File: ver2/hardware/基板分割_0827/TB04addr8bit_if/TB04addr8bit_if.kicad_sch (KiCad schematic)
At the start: 12 parts, among them J101 USB_C_Receptacle_PowerOnly_6P, SW101 SW_SPDT, U101 74LS157, U102 74HC138

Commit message: ver2: 3分割で丸ごと不要なシートを削除(ctrl 3・alu 8・if 9シート)
階層ピン0のシートのみ削除。RS00/RS01は22ピンあるためGUI待ち。
差分は追加0行の純削除。

Co-Authored-By: Claude Opus 5 <noreply@anthropic.com>
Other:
- removed sheet Decoder
- removed sheet InterFace
- removed sheet PC_aluMux (4 ページ)
- removed sheet ROM_ALU
- removed sheet addrDecord
- removed sheet addrMUX
- removed sheet gates
- removed sheet ram
- removed sheet sp

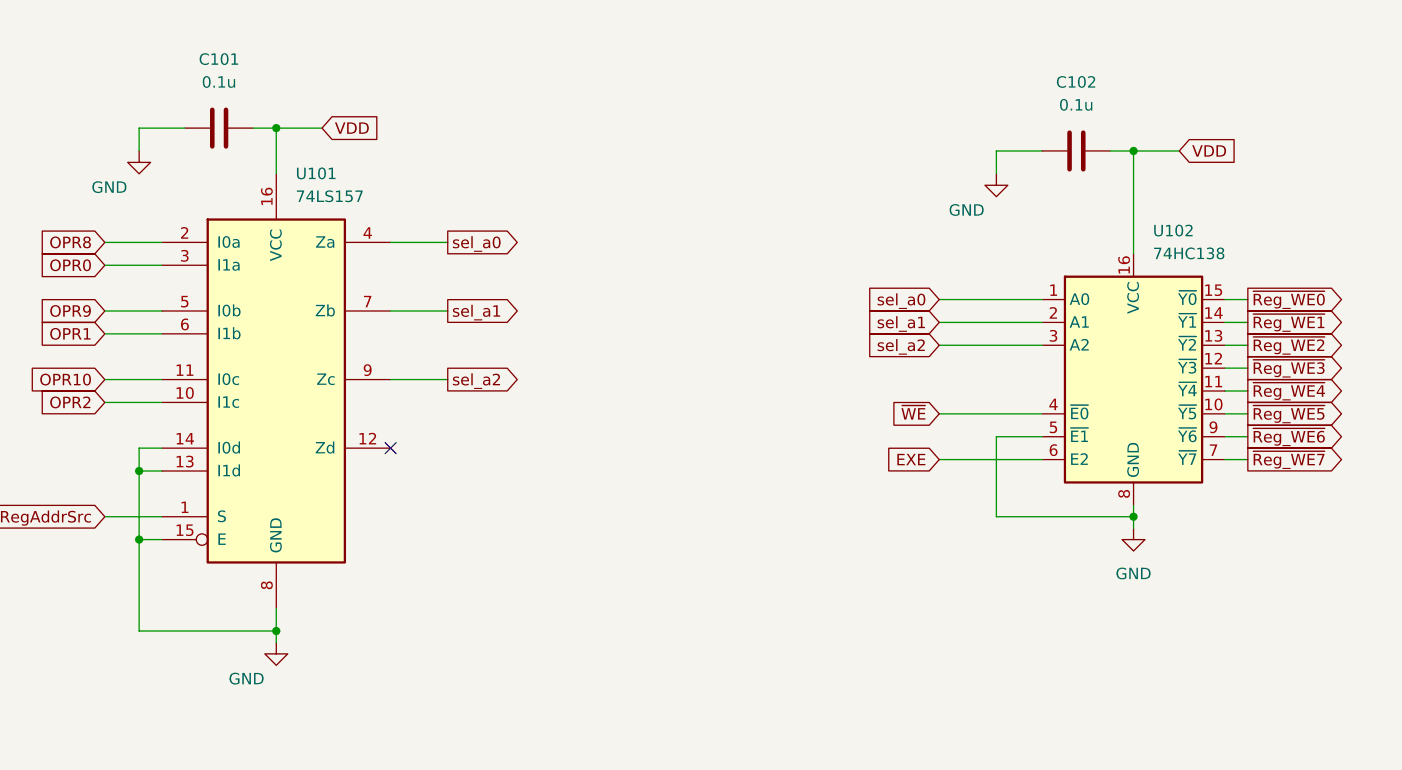
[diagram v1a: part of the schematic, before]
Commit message: ver2: 3分割で他基板側のICを削除(ctrl 9・alu 15・if 2個)
削除前にまたぎ本数(37/20)で割り当てを検算。kicad-cliのパース通過を確認。

Co-Authored-By: Claude Opus 5 <noreply@anthropic.com>
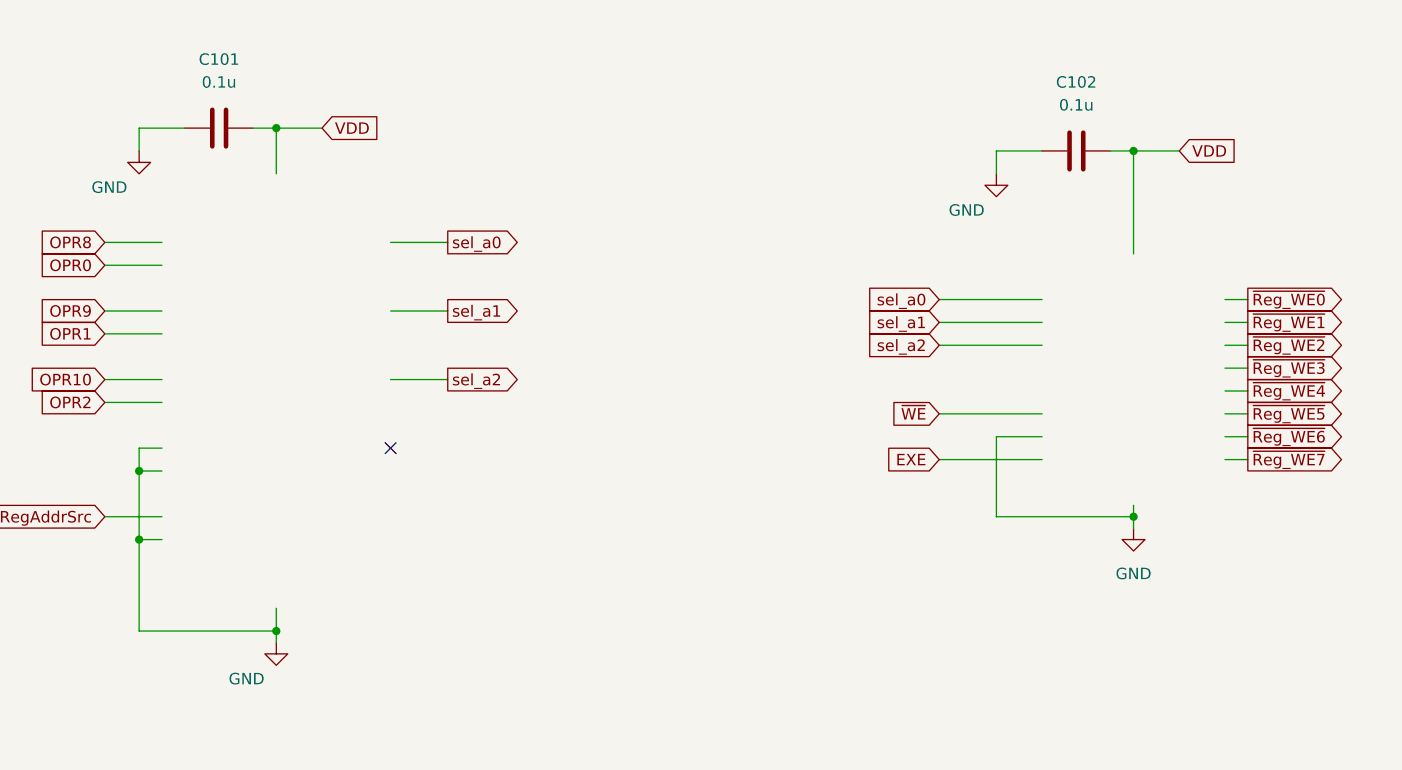
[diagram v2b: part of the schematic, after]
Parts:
- removed U101: 74LS157, Package_DIP:DIP-16_W7.62mm_Socket, symbol 74xx:74LS157
- removed U102: 74HC138, Package_DIP:DIP-16_W7.62mm_Socket, symbol 74xx:74HC138
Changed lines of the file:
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@@
-	)
-	(symbol
-		(lib_id "74xx:74LS157")
-		(at 171.45 146.05 0)
-		(unit 1)
-		(body_style 1)
-		(exclude_from_sim no)
-		(in_bom yes)
-		(on_board yes)
-		(in_pos_files yes)
-		(dnp no)
-		(fields_autoplaced yes)
-		(property "Reference" "U101"
-			(at 173.5933 123.19 0)
-			(show_name no)
-			(do_not_autoplace no)
-			(effects
-				(font
-					(size 1.27 1.27)
-				)
-				(justify left)
-			)
-		)
-		(property "Value" "74LS157"
-			(at 173.5933 125.73 0)
-			(show_name no)
-			(do_not_autoplace no)
-			(effects
-				(font
-					(size 1.27 1.27)
-				)
-				(justify left)
-			)
-		)
-		(property "Footprint" "Package_DIP:DIP-16_W7.62mm_Socket"
-			(at 171.45 146.05 0)
-			(hide yes)
-			(show_name no)
-			(do_not_autoplace no)
-			(effects
-				(font
-					(size 1.27 1.27)
-				)
-			)
-		)
-		(property "Datasheet" "http://www.ti.com/lit/gpn/sn74LS157"
-			(at 171.45 146.05 0)
-			(hide yes)
-			(show_name no)
-			(do_not_autoplace no)
-			(effects
-				(font
-					(size 1.27 1.27)
-				)
-			)
-		)
-		(property "Description" "Quad 2 to 1 line Multiplexer"
-			(at 171.45 146.05 0)
-			(hide yes)
-			(show_name no)
-			(do_not_autoplace no)
-			(effects
-				(font
-					(size 1.27 1.27)
-				)
-			)
-		)
-		(pin "4"
-		)
-		(pin "12"
-		)
-		(pin "6"
-		)
-		(pin "9"
-		)
-		(pin "3"
-		)
-		(pin "16"
-		)
-		(pin "8"
-		)
-		(pin "10"
-		)
-		(pin "11"
-		)
-		(pin "5"
-		)
-		(pin "13"
-		)
-		(pin "1"
-		)
-		(pin "2"
-		)
-		(pin "7"
-		)
-		(pin "14"
-		)
-		(pin "15"
-		)
-		(instances
-			(project "TB04addr8bit_if"
-				(path "/d176c79b-dced-4d01-bcec-7dfd676fcfc2"
-					(reference "U101")
-					(unit 1)
-				)
-			)
-		)
 	)
 	(symbol
@@
 					(unit 1)
 				)
-			)
-		)
-	)
-	(symbol
-		(lib_id "74xx:74HC138")
-		(at 266.7 147.32 0)
-		(unit 1)
-		(body_style 1)
-		(exclude_from_sim no)
-		(in_bom yes)
-		(on_board yes)
-		(in_pos_files yes)
-		(dnp no)
-		(fields_autoplaced yes)
-		(property "Reference" "U102"
-			(at 268.8433 129.54 0)
-			(show_name no)
-			(do_not_autoplace no)
-			(effects
-				(font
-					(size 1.27 1.27)
-				)
-				(justify left)
-			)
-		)
-		(property "Value" "74HC138"
-			(at 268.8433 132.08 0)
-			(show_name no)
-			(do_not_autoplace no)
-			(effects
-				(font
-					(size 1.27 1.27)
-				)
-				(justify left)
-			)
-		)
-		(property "Footprint" "Package_DIP:DIP-16_W7.62mm_Socket"
-			(at 266.7 147.32 0)
-			(hide yes)
-			(show_name no)
-			(do_not_autoplace no)
-			(effects
-				(font
-					(size 1.27 1.27)
-				)
-			)
-		)
-		(property "Datasheet" "http://www.ti.com/lit/ds/symlink/cd74hc238.pdf"
-			(at 266.7 147.32 0)
-			(hide yes)
-			(show_name no)
-			(do_not_autoplace no)
-			(effects
-				(font
-					(size 1.27 1.27)
-				)
-			)
-		)
-		(property "Description" "3-to-8 line decoder/multiplexer inverting, DIP-16/SOIC-16/SSOP-16"
-			(at 266.7 147.32 0)
-			(hide yes)
-			(show_name no)
-			(do_not_autoplace no)
-			(effects
-				(font
-					(size 1.27 1.27)
-				)
-			)
-		)
-		(pin "11"
-		)
-		(pin "1"
-		)
-		(pin "8"
-		)
-		(pin "5"
-		)
-		(pin "14"
-		)
-		(pin "10"
-		)
-		(pin "2"
-		)
-		(pin "4"
-		)
-		(pin "13"
-		)
-		(pin "3"
-		)
-		(pin "7"
-		)
-		(pin "6"
-		)
-		(pin "16"
-		)
-		(pin "12"
-		)
-		(pin "9"
-		)
-		(pin "15"
-		)
-		(instances
-			(project "TB04addr4bit"
-				(path "/4ea1f5c4-c9b0-4258-a3d4-23d6760fc0c5"
-					(reference "U15")
-					(unit 1)
-				)
-			)
-			(project "TB04addr8bit_if"
-				(path "/d176c79b-dced-4d01-bcec-7dfd676fcfc2"
-					(reference "U102")
-					(unit 1)
-				)

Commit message: ver2: 3分割でシート内の不要部品・配線を削除(検証合格)／キャリアを0827へコピー
- 制御34・演算25・IF10=IC69でマスターと一致、部品の取りこぼし0
- ピン-ネット署名の変化0件=誤って線を切った箇所なし
- またぐ信号は制御/演算35・IF/制御18で手順書の表と過不足ゼロ

Co-Authored-By: Claude Opus 5 <noreply@anthropic.com>
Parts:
- removed C101, C102: 0.1u, Capacitor_THT:C_Disc_D4.3mm_W1.9mm_P5.00mm, symbol Device:C
- added J1602: Screw_Terminal_01x02, symbol Connector:Screw_Terminal_01x02
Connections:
- net GND: now also J1602.2 (Pin_2)
- net VDD: now also J1602.1 (Pin_1)
- no-connect marks 6 -> 5
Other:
- removed sheet RS00
- removed sheet RS01
- moved on the sheet: C103, C104, D101, J101, R101, R102, R103, SW101

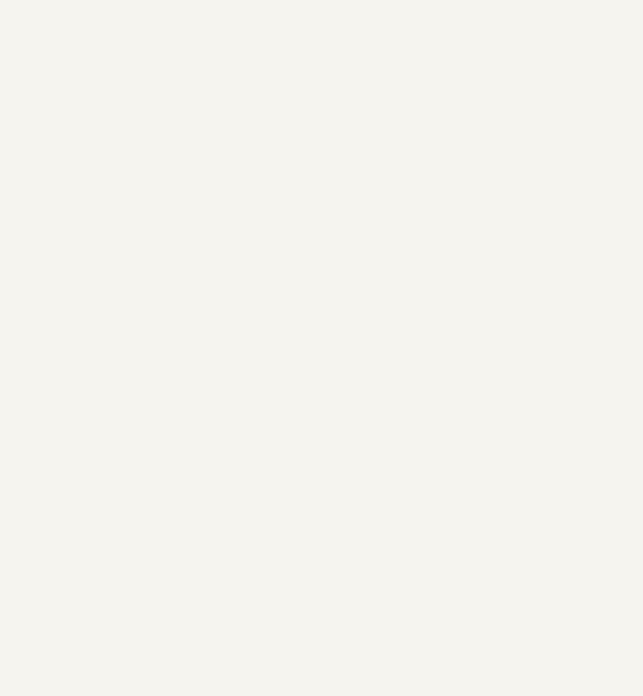
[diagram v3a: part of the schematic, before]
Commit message: ver2: 作業中の区切り(制御板のJ805-808を削除・制御板とIF板にケーブル用2x20を配置)
- 制御板: InterFaceからJ805-808を削除、J801-804(命令表示4桁)は残す
- 制御板ルートに2x20を3個、IF板ルートに2x20を1個
- 結線とai-reviewはこれから

Co-Authored-By: Claude Opus 5 <noreply@anthropic.com>
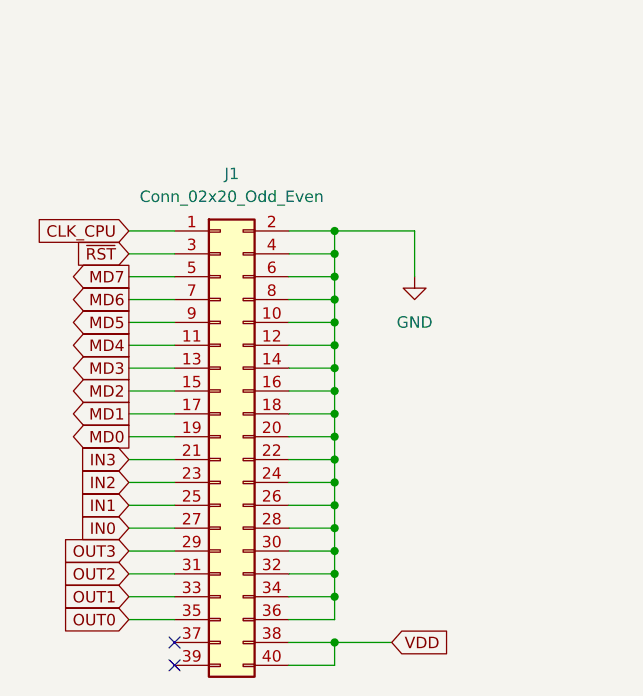
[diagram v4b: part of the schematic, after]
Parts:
- added J1: Conn_02x20_Odd_Even, symbol Connector_Generic:Conn_02x20_Odd_Even
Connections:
- net GND: now also J1.10 (Pin_10), J1.12 (Pin_12), J1.14 (Pin_14), J1.16 (Pin_16), J1.18 (Pin_18), J1.2 (Pin_2), J1.20 (Pin_20), J1.22 (Pin_22), J1.24 (Pin_24), J1.26 (Pin_26), J1.28 (Pin_28), J1.30 (Pin_30), J1.32 (Pin_32), J1.34 (Pin_34), J1.36 (Pin_36), J1.4 (Pin_4), J1.6 (Pin_6), J1.8 (Pin_8)
- net VDD: now also J1.38 (Pin_38), J1.40 (Pin_40)
- new net CLK_CPU: J1.1 (Pin_1)
- new net IN0: J1.27 (Pin_27)
- new net IN1: J1.25 (Pin_25)
- new net IN2: J1.23 (Pin_23)
- new net IN3: J1.21 (Pin_21)
- new net MD0: J1.19 (Pin_19)
- new net MD1: J1.17 (Pin_17)
- new net MD2: J1.15 (Pin_15)
- new net MD3: J1.13 (Pin_13)
- new net MD4: J1.11 (Pin_11)
- new net MD5: J1.9 (Pin_9)
- new net MD6: J1.7 (Pin_7)
- new net MD7: J1.5 (Pin_5)
- new net OUT0: J1.35 (Pin_35)
- new net OUT1: J1.33 (Pin_33)
- new net OUT2: J1.31 (Pin_31)
- new net OUT3: J1.29 (Pin_29)
- new net ~{RST}: J1.3 (Pin_3)
- no-connect marks 5 -> 7

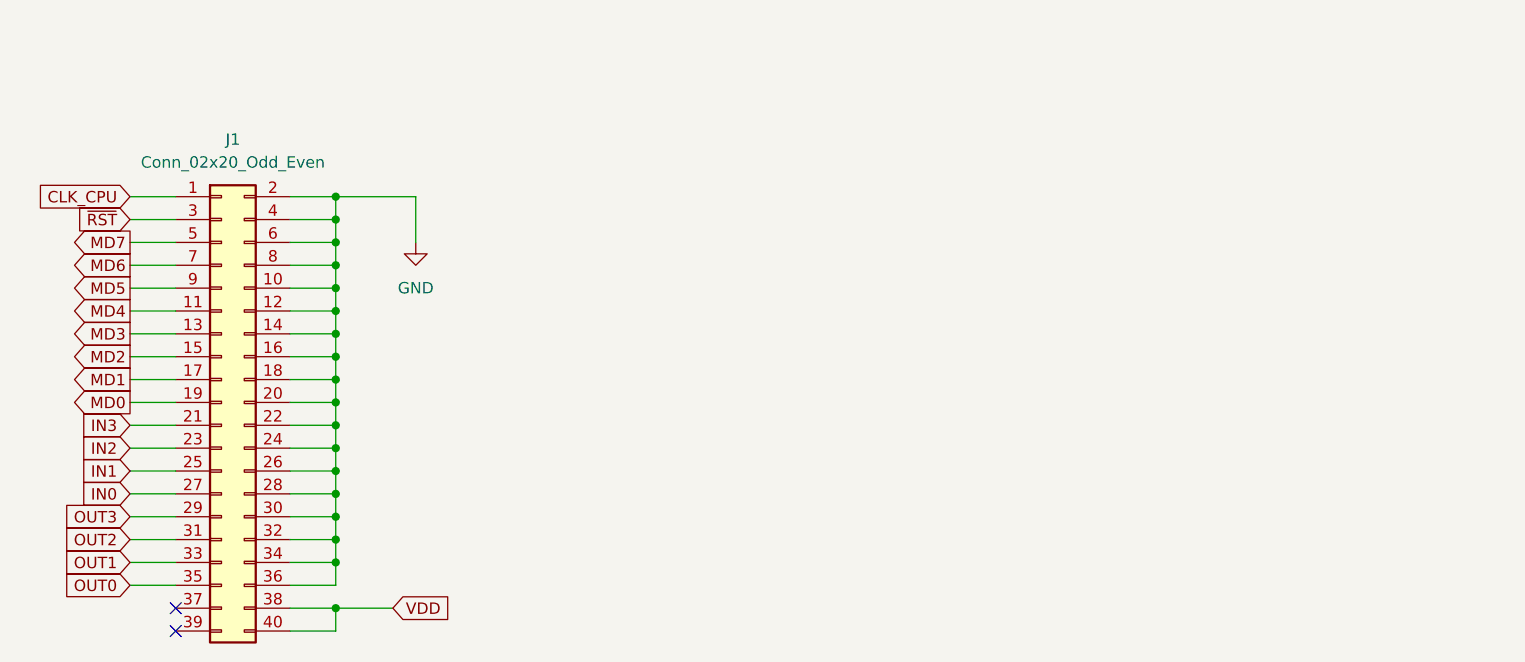
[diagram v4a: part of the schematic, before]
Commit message: ver2: 3分割にケーブル用・キャリア用コネクタを実装(検証全項目合格)
- ケーブル両端のピン割り当て100ピン全数一致、手順書の表とも不一致0
- またぐ47信号すべてコネクタに出ている(未接続0)
- isolated_pin_label 34→0、pin_not_driven 29→0

Co-Authored-By: Claude Opus 5 <noreply@anthropic.com>
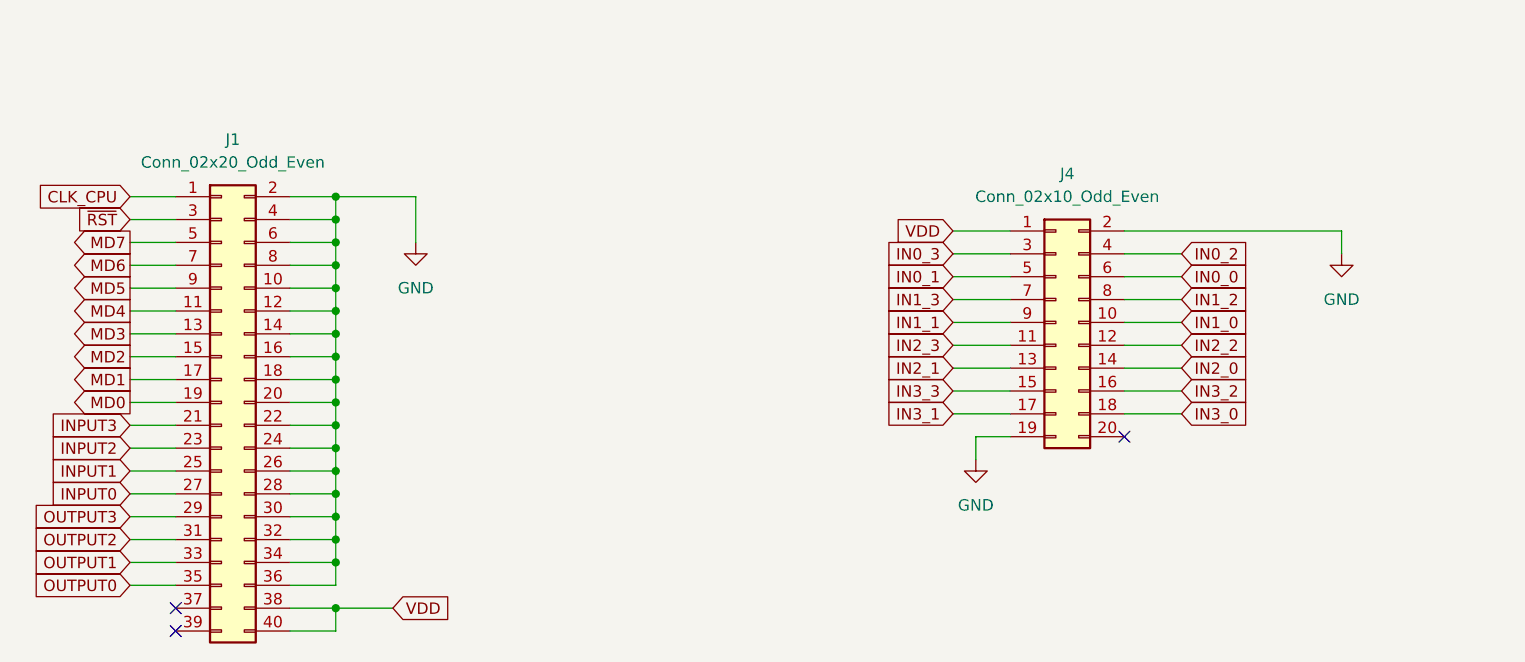
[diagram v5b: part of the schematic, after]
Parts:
- added J4: Conn_02x10_Odd_Even, symbol Connector_Generic:Conn_02x10_Odd_Even
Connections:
- net GND: now also J4.19 (Pin_19), J4.2 (Pin_2)
- net VDD: now also J4.1 (Pin_1)
- net IN0 renamed INPUT0
- net IN1 renamed INPUT1
- net IN2 renamed INPUT2
- net IN3 renamed INPUT3
- net OUT0 renamed OUTPUT0
- net OUT1 renamed OUTPUT1
- net OUT2 renamed OUTPUT2
- net OUT3 renamed OUTPUT3
- new net IN0_0: J4.6 (Pin_6)
- new net IN0_1: J4.5 (Pin_5)
- new net IN0_2: J4.4 (Pin_4)
- new net IN0_3: J4.3 (Pin_3)
- new net IN1_0: J4.10 (Pin_10)
- new net IN1_1: J4.9 (Pin_9)
- new net IN1_2: J4.8 (Pin_8)
- new net IN1_3: J4.7 (Pin_7)
- new net IN2_0: J4.14 (Pin_14)
- new net IN2_1: J4.13 (Pin_13)
- new net IN2_2: J4.12 (Pin_12)
- new net IN2_3: J4.11 (Pin_11)
- new net IN3_0: J4.18 (Pin_18)
- new net IN3_1: J4.17 (Pin_17)
- new net IN3_2: J4.16 (Pin_16)
- new net IN3_3: J4.15 (Pin_15)
- no-connect marks 7 -> 8

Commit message: ver2: 3分割のフットプリント設定完了・取付穴を追加・PCBを作り直し
- 新規コネクタ11件のフットプリントを設定(2x20/2x10ピンソケット・端子台)
- 演算板/制御板/キャリアに取付穴MountingHole_Pad×4とGNDを追加(M3・パッド付きビア)
- 3枚のPCBをコピー元マスターのレイアウトを一掃して作り直し(配置前・配線0)
- 階層から外れて残っていたRS00/RS01.kicad_sch(制御板・IF板)を削除

検証: フットプリント未設定0件、回路図とPCBの参照番号の集合差分0
(演算102/制御101/IF127/キャリア14)、回路図の電気的変更なし

Co-Authored-By: Claude Opus 5 <noreply@anthropic.com>
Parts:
- J1: footprint (none) -> Connector_PinSocket_2.54mm:PinSocket_2x20_P2.54mm_Vertical
- J1602: footprint (none) -> TerminalBlock:TerminalBlock_MaiXu_MX126-5.0-02P_1x02_P5.00mm
- J4: footprint (none) -> Connector_PinSocket_2.54mm:PinSocket_2x10_P2.54mm_Vertical
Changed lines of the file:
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@@
 			)
 		)
-		(property "Footprint" ""
+		(property "Footprint" "Connector_PinSocket_2.54mm:PinSocket_2x10_P2.54mm_Vertical"
 			(at 241.3 177.8 0)
 			(hide yes)
@@
 			)
 		)
-		(property "Footprint" ""
+		(property "Footprint" "Connector_PinSocket_2.54mm:PinSocket_2x20_P2.54mm_Vertical"
 			(at 148.59 186.69 0)
 			(hide yes)
@@
 			)
 		)
-		(property "Footprint" ""
+		(property "Footprint" "TerminalBlock:TerminalBlock_MaiXu_MX126-5.0-02P_1x02_P5.00mm"
 			(at 144.78 106.68 0)
 			(hide yes)
